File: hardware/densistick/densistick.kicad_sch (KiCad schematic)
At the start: 58 parts, among them J1 Cable, SW1 SW_Push, U1 TSL2585, U2 USBLC6-2SC6, U3 MIC4812, U4 FT260Q, U5 MIC5365-1.8YC5, U6 CAT24C08, U7 MCP4017-104E/LT

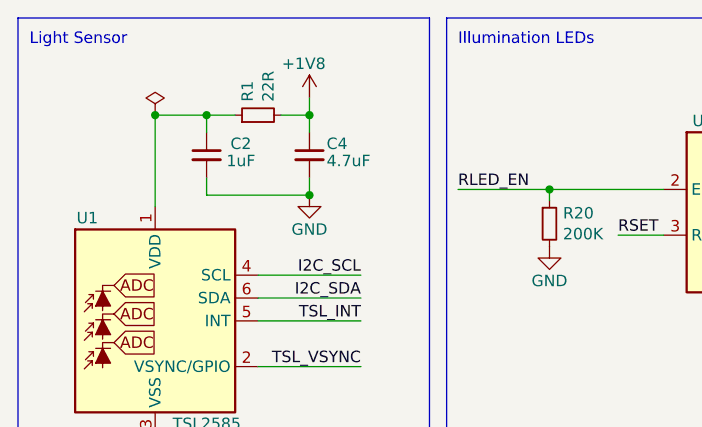
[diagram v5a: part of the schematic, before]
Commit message: Update KiCad files to v9 format
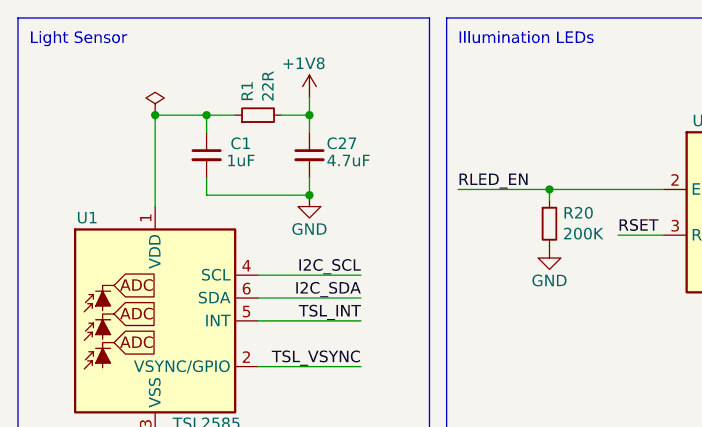
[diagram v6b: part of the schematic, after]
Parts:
- renumbered C2 to C1, C4 to C27

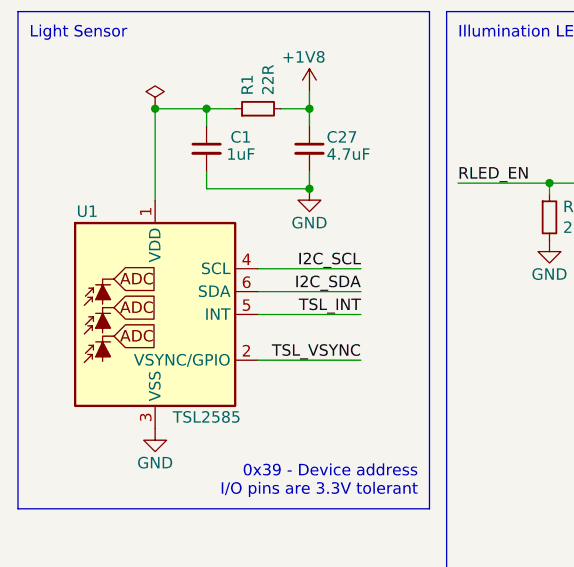
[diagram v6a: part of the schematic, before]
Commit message: Change light sensor on peripherals
Ref #85
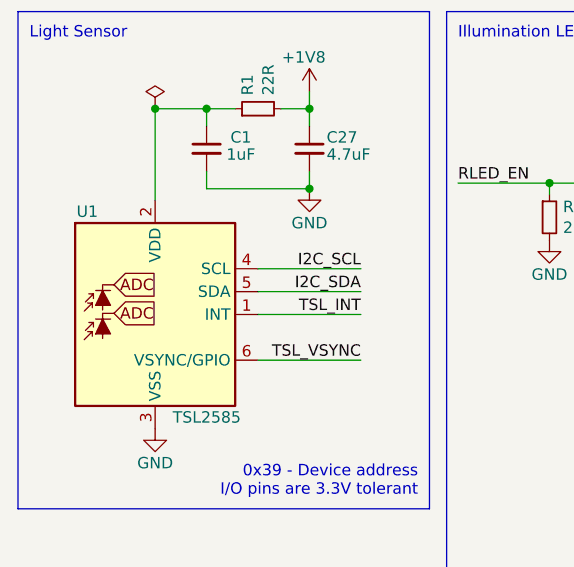
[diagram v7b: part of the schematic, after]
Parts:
- U1: symbol Project:TSL2585 -> Project:TSL2522; Manufacturer PN TSL25853PM -> TSL25223; Supplier Digi-Key -> Mouser; Supplier PN 4991-TSL25853PMCT-ND -> 985-TSL25223OLGA6
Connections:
- net I2C_SDA: now also U1.5 (SDA); no longer U1.6 (SDA)
- net TSL_INT: now also U1.1 (INT); no longer U1.5 (INT)
- net TSL_VSYNC: now also U1.6 (VSYNC/GPIO); no longer U1.2 (VSYNC/GPIO)
- net at C1.1, R1.1: now also U1.2 (VDD); no longer U1.1 (VDD)
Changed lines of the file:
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@@
 	(title_block
 		(title "Printalyzer DensiStick")
-		(date "2024-12-03")
-		(rev "B")
+		(date "2025-04-30")
+		(rev "C")
 		(company "Dektronics, Inc.")
 		(comment 1 "Derek Konigsberg <dkonigsberg@dektronics.com>")
@@
 	)
 	(symbol
-		(lib_id "Project:TSL2585")
+		(lib_id "Project:TSL2522")
 		(at 29.845 48.26 0)
 		(unit 1)
@@
 		)
 		(property "Footprint" "lib_fp:AMS_TSL2585_OLGA-6_2x1mm_P0.65mm"
-			(at 31.115 59.69 0)
+			(at 29.845 73.152 0)
 			(effects
 				(font
@@
 			)
 		)
-		(property "Datasheet" "https://ams.com/documents/20143/6148289/TSL2585_DS001043_4-00.pdf"
-			(at 29.845 72.39 0)
+		(property "Datasheet" "https://look.ams-osram.com/m/297a255d37b15c/original/TSL2522-Highly-sensitive-ambient-light-sensor-with-light-flicker-detection.pdf"
+			(at 29.845 78.232 0)
 			(effects
 				(font
@@
 			)
 		)
-		(property "Description" "AMBIENT LIGHT SENSOR"
-			(at 29.845 48.26 0)
+		(property "Description" "Light sensor with Photopic and IR detection, I2C interface, 1.8V, FN"
+			(at 29.845 75.692 0)
 			(effects
 				(font
@@
 			)
 		)
-		(property "Manufacturer PN" "TSL25853PM"
+		(property "Manufacturer PN" "TSL25223"
 			(at 29.845 48.26 0)
 			(effects
@@
 			)
 		)
-		(property "Supplier" "Digi-Key"
+		(property "Supplier" "Mouser"
 			(at 29.845 48.26 0)
 			(effects
@@
 			)
 		)
-		(property "Supplier PN" "4991-TSL25853PMCT-ND"
+		(property "Supplier PN" "985-TSL25223OLGA6"
 			(at 29.845 48.26 0)
 			(effects

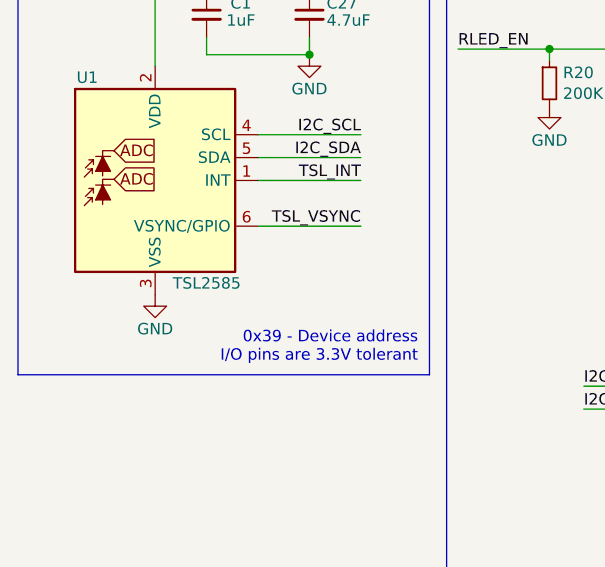
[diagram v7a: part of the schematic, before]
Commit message: Fix component value and some symbol/footprint updates
Forgot to change the "Value" field of the light sensor when switching it
from the TSL2585 to the TSL2522.

Also pulled in some minor KiCad changes to symbols and footprints, all
of which affect metadata and do not change the board layout itself.
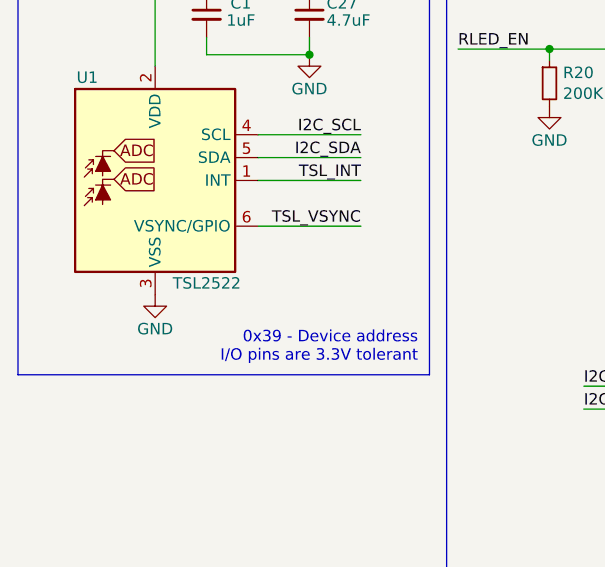
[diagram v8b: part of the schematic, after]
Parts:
- U1: value TSL2585 -> TSL2522
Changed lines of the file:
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@@
 			)
 		)
-		(property "Value" "TSL2585"
+		(property "Value" "TSL2522"
 			(at 39.37 59.69 0)
 			(effects
